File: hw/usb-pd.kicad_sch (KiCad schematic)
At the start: 15 parts, among them J1901 Amphenol 10167129, Q1901 SQJ433EP, U1901 STUSB4500QTR

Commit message: Ready for first schematic review with Claude.ai
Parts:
- renumbered C1901 to C2001, C1902 to C2002, C1903 to C2003, C1904 to C2004, D1901 to D2001, J1901 to J2001, Q1901 to Q2001, R1901 to R2001, R1902 to R2002, R1903 to R2003, R1904 to R2004, R1905 to R2005, R1906 to R2006, R1907 to R2007, U1901 to U2001
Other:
- company: (none) -> WB7NAB
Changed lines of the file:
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@@
 		(title "USB-PD")
 		(date "2025-10-28")
+		(company "WB7NAB")
+		(comment 1 "Alan Mimms")
 	)

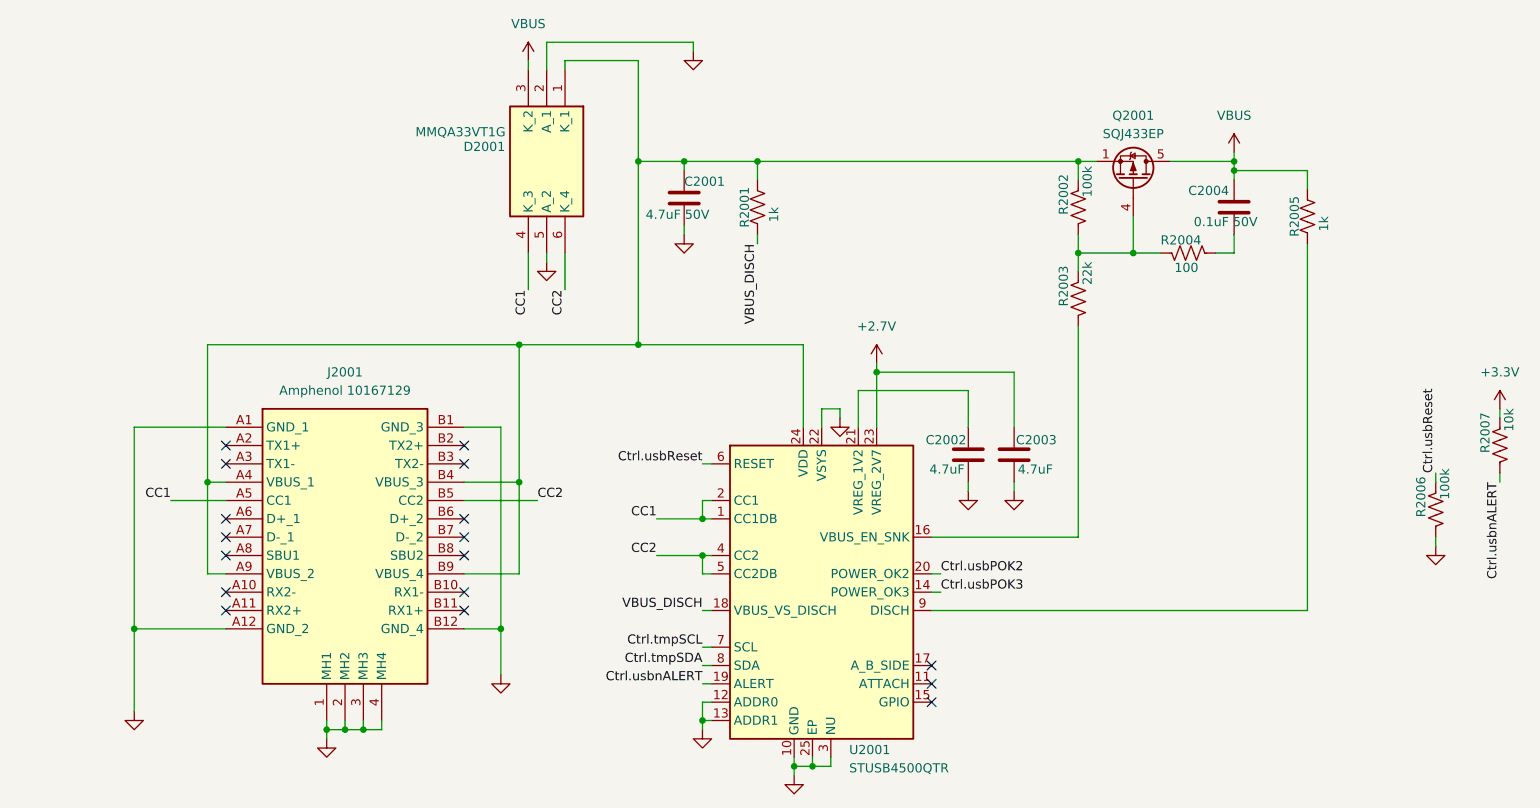
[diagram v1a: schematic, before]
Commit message: Revamp the rx preselector to achieve general coverage from 1MHz to 30MHz with overlapping bands
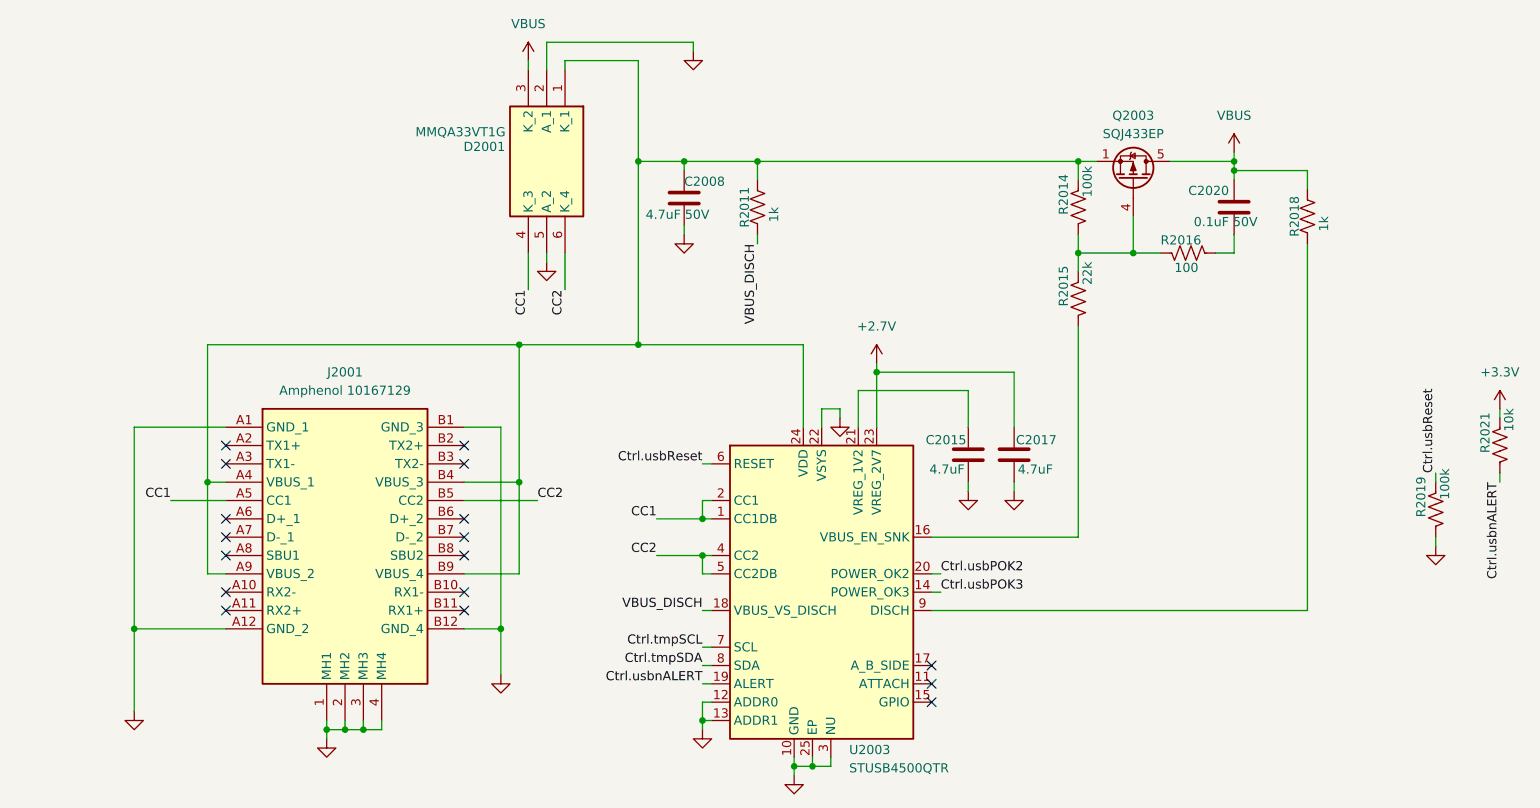
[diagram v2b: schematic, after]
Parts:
- C2008: renamed from C2001; footprint (none) -> Capacitor_SMD:C_1206_3216Metric
- C2015: renamed from C2002; footprint (none) -> Capacitor_SMD:C_0805_2012Metric
- C2017: renamed from C2003; footprint (none) -> Capacitor_SMD:C_0805_2012Metric
- C2020: renamed from C2004; footprint (none) -> Capacitor_SMD:C_1206_3216Metric
- D2001: footprint SOP95P275X110-6N -> Package_TO_SOT_SMD:SC-74-6_1.55x2.9mm_P0.95mm
- renumbered Q2001 to Q2003, R2001 to R2011, R2002 to R2014, R2003 to R2015, R2004 to R2016, R2005 to R2018, R2006 to R2019, R2007 to R2021, U2001 to U2003

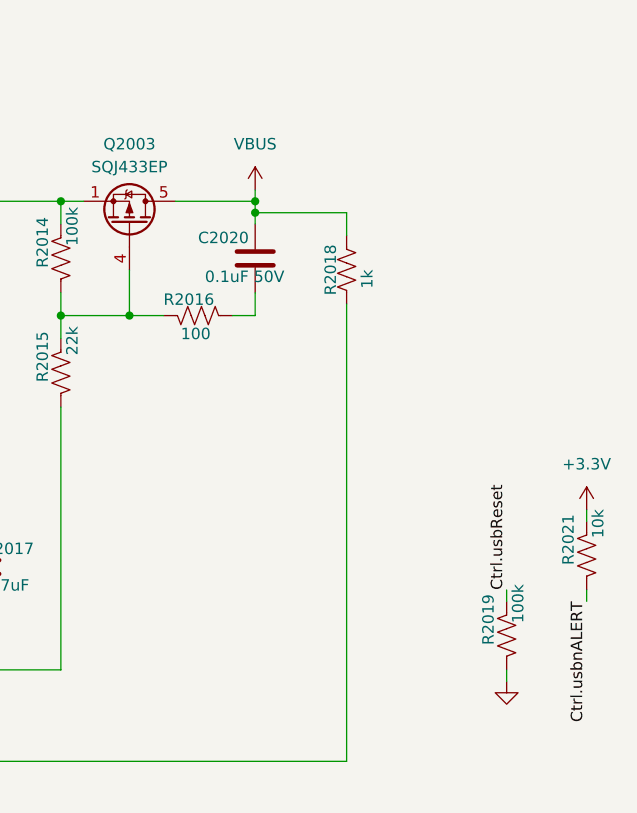
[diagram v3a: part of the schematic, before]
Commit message: Removed PA tanks. LPFs are now 7th order Chebyshev and we are better than -70dBc. Added 0R to power rails for measuring and other testing (did not dare do that for Veer). PCB is now grouped by function to get ready for layout. Still need to verify and set C working voltage levels and choose L and C components for the LPFs. Now using smaller relays at a slight cost premium.
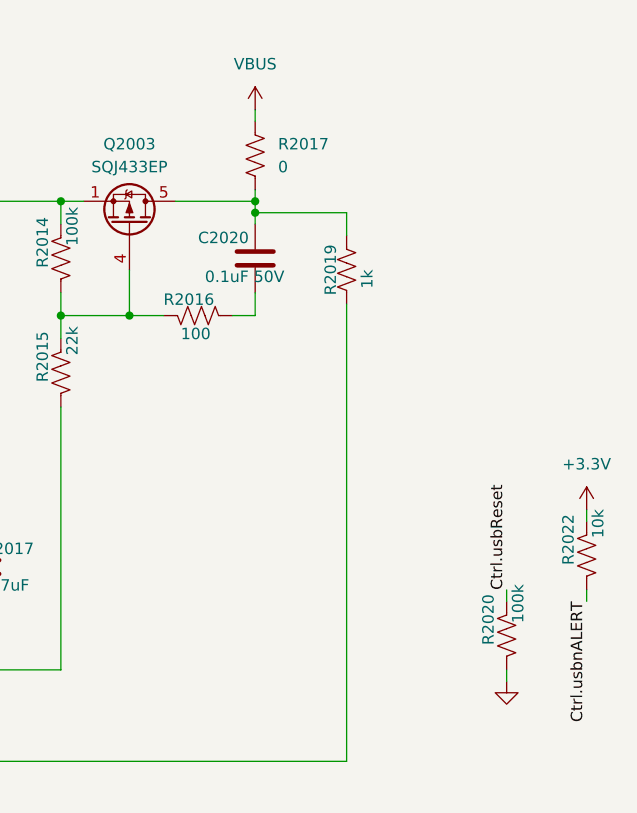
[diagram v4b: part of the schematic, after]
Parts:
- added R2017: 0, Resistor_SMD:R_1206_3216Metric, symbol Device:R_US
- renumbered R2018 to R2019, R2019 to R2020, R2021 to R2022
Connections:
- net VBUS: now also R2017.1; no longer C2020.1, Q2003.5 (D), R2019.1
- new net: C2020.1, Q2003.5 (D), R2017.2, R2019.1

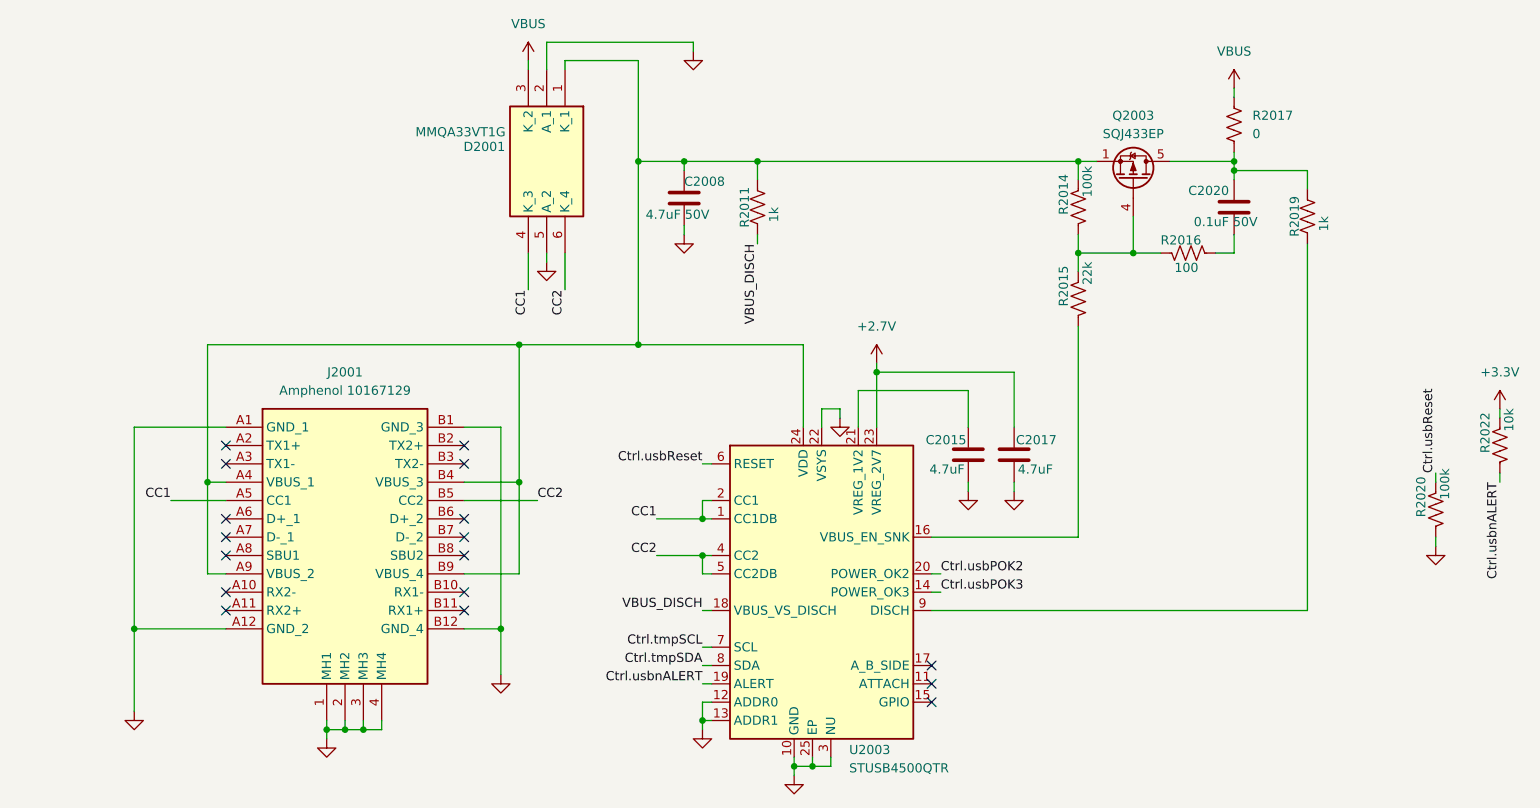
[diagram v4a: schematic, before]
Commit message: Redefine LPFs to combine bands to save on filter count and components and area now that we have 7th order Chebyshev filters. Define components and footprints for inductors in the LPFs. Lose the old pa-tanks page.
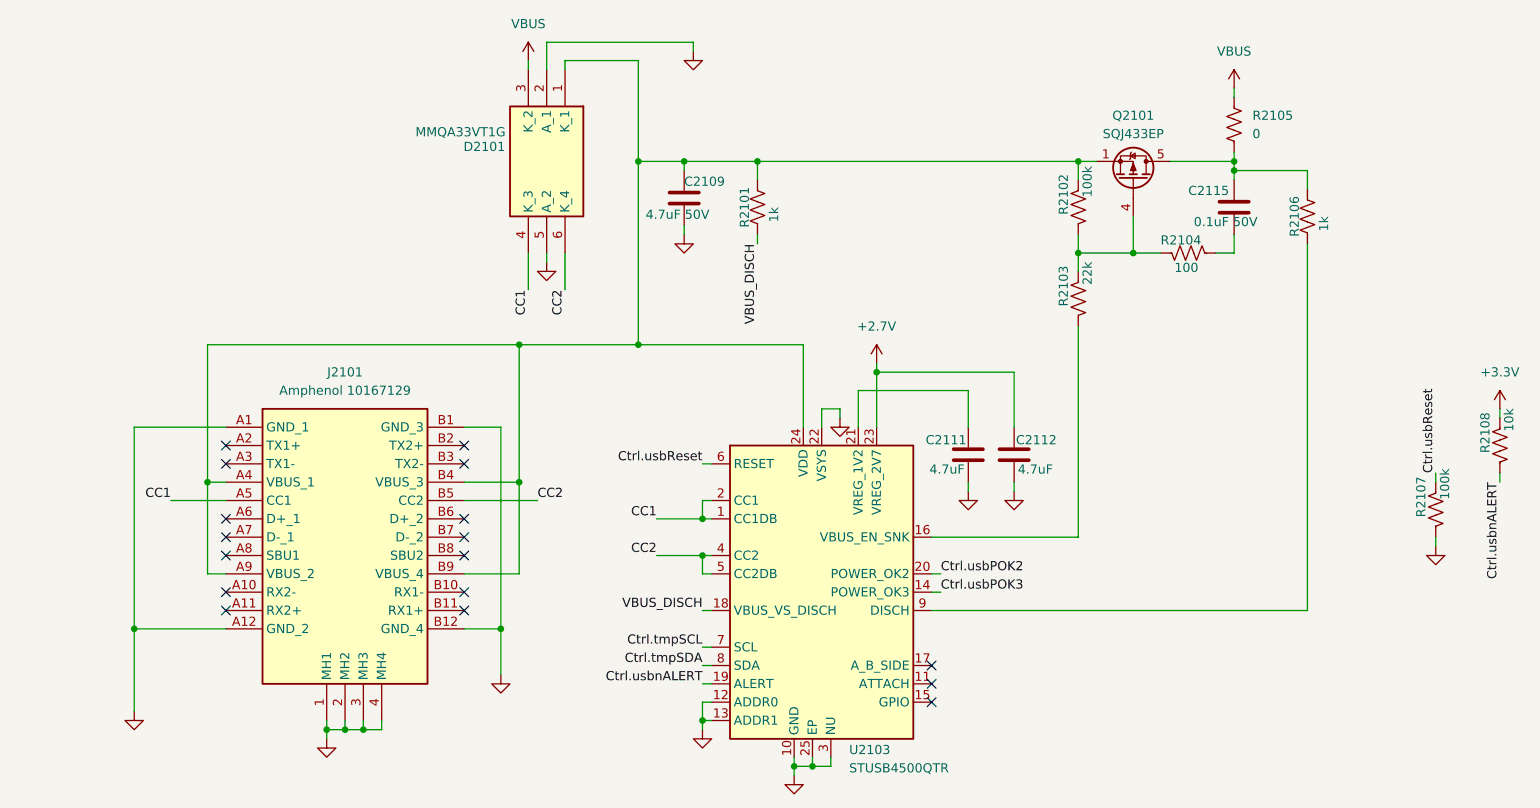
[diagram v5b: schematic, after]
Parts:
- renumbered C2008 to C2109, C2015 to C2111, C2017 to C2112, C2020 to C2115, D2001 to D2101, J2001 to J2101, Q2003 to Q2101, R2011 to R2101, R2014 to R2102, R2015 to R2103, R2016 to R2104, R2017 to R2105, R2019 to R2106, R2020 to R2107, R2022 to R2108, U2003 to U2103

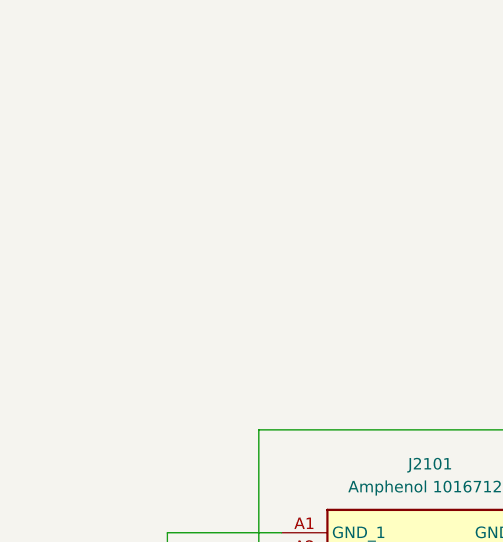
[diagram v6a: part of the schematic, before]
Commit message: Massive (simple) fixes to connect Ctrl bus across sheets - I had misunderstood how that works.
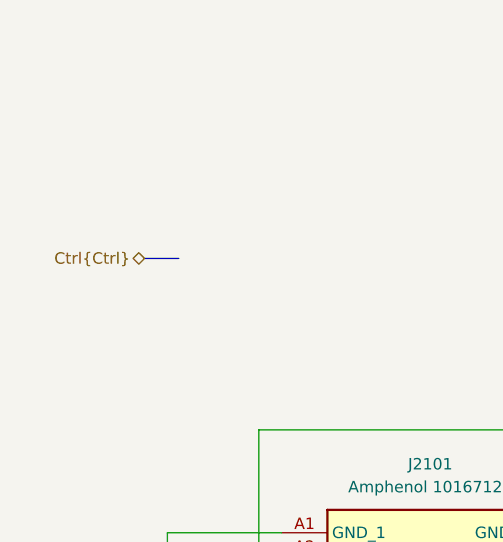
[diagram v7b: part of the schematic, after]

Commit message: Started routing again with real board outline. Placement first, then routing, really.
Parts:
- J2101: value Amphenol 10167129 -> USB C power only; footprint Library:1016712900011LF -> Library:UJ20CHGMSMT4P16TR; symbol Library:USB-C-3.2g2 -> Library:UJ20-C-H-G-MSMT-4-P16-TR; Height 10.23 -> 3.36; Manufacturer_Name Amphenol Communications Solutions -> Same Sky; Manufacturer_Part_Number 10167129-00011LF -> UJ20-C-H-G-MSMT-4-P16-TR; Mouser Part Number (none) -> 179-UJ20CHGMSMT4P16T; Mouser Price/Stock (none) -> https://www.mouser.co.uk/ProductDetail/Same-Sky/UJ20-C-H-G-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
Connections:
- net GND: no longer J2101.A12 (GND_2), J2101.B12 (GND_4)
- net at C2109.1, D2101.1 (K_1), J2101.A4 (VBUS_1)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: no longer J2101.A9 (VBUS_2), J2101.B9 (VBUS_4)
- no-connect marks 17 -> 9
